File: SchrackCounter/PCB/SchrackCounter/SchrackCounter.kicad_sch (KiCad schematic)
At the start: 0 parts

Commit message: fix?
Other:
- note added: "FIX FONTS AND SYMBOLS"
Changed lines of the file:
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@@
 		(comment 1 "SAVVA POPOV")
+	)
+	(text "FIX FONTS AND SYMBOLS"
+		(exclude_from_sim no)
+		(at 86.106 173.736 0)
+		(effects
+			(font
+				(size 5 5)
+			)
+		)
 	)
 	(symbol
@@
 		)
 		(instances
-			(project ""
+			(project "SchrackCounter"
 				(path "/d96f2ffc-3f4c-4f71-b693-29f6b8c3245d"
 					(reference "#G1")

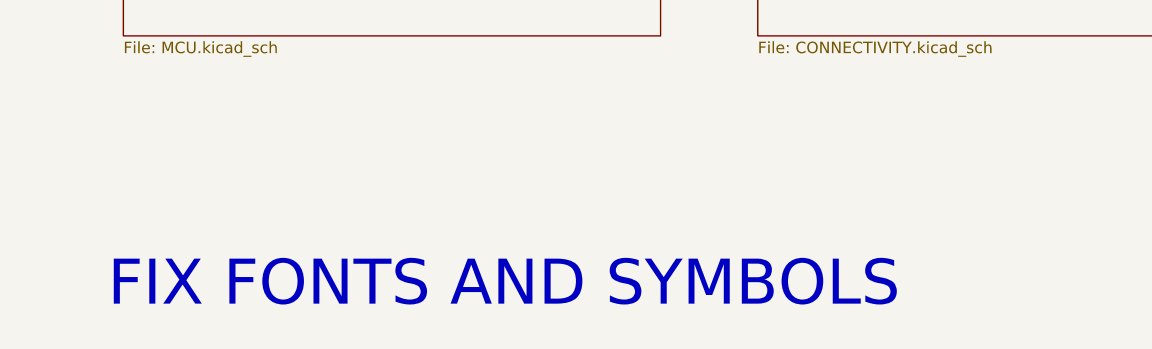
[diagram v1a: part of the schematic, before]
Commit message: PCB update, minor schematic update
PCB routing update, 7segment routing, and minor changes to the 7segments in schematic
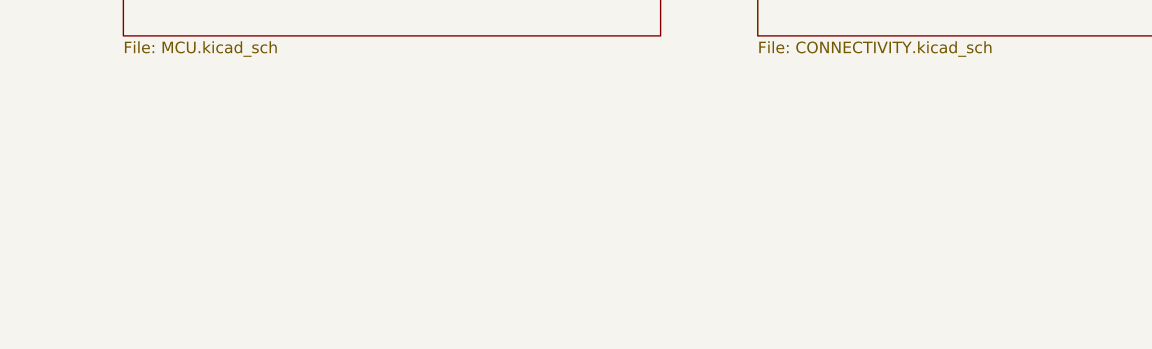
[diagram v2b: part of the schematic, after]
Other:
- note removed: "FIX FONTS AND SYMBOLS"
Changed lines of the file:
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@@
 		(comment 1 "SAVVA POPOV")
-	)
-	(text "FIX FONTS AND SYMBOLS"
-		(exclude_from_sim no)
-		(at 86.106 173.736 0)
-		(effects
-			(font
-				(size 5 5)
-			)
-		)
 	)
 	(symbol
@@
 			(effects
 				(font
+					(face "Bahnschrift")
 					(size 4 4)
 					(color 0 0 0 1)
@@
 			(effects
 				(font
+					(face "Bahnschrift")
 					(size 4 4)
 					(color 0 0 0 1)
@@
 			(effects
 				(font
-					(size 4 4)
-					(color 0 0 0 1)
+					(face "Bahnschrift")
+					(size 4 4)
+					(color 0 0 0 1)
